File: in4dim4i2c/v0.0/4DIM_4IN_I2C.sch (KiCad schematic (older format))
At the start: 71 parts, among them IC1 ATTINY2313-P, IC2 MOC3020M, IC3 MOC3020M, IC4 MOC3020M, IC5 MOC3020M, P1 CONN_2, P10 CONN_2, P2 CONN_2, P4 CONN_5, P5 CONN_5, P6 CONN_5, P7 CONN_2, P8 CONN_2, P9 CONN_2, U1 TRIAC, U2 TRIAC, U3 TRIAC, U4 TRIAC

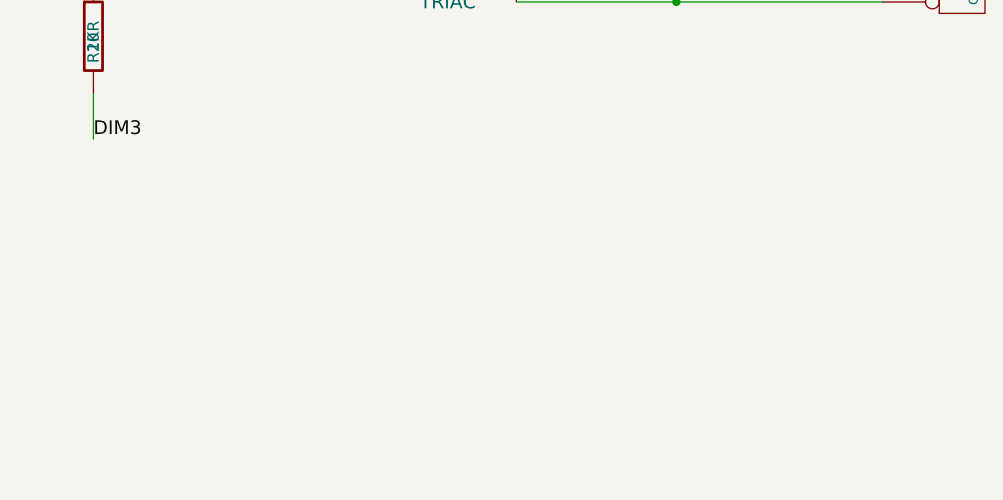
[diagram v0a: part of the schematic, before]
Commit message: Add zero cross detection circuit and P620 footprint
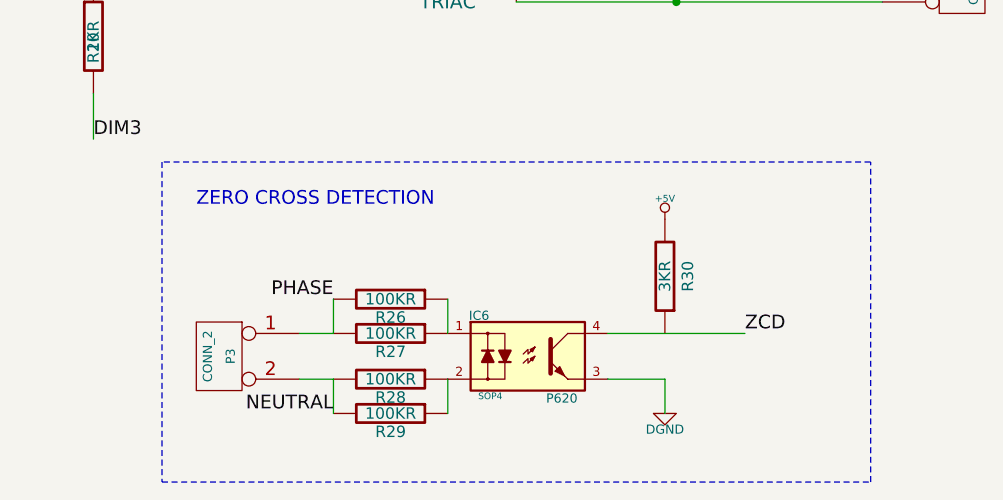
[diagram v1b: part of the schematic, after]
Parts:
- added IC6: P620, SOP4, symbol TLP290
- added P3: CONN_2, symbol CONN_2
- added R26, R27, R28, R29: 100KR, symbol R
- added R30: 3KR, symbol R
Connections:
- net +5V: now also R30.2
- net DGND: now also IC6.3
- net ZCD: now also IC6.4
- new net: IC6.1, R26.1, R27.1
- new net: IC6.2, R28.1, R29.1
- new net NEUTRAL: P3.2 (PM), R28.2, R29.2
- new net PHASE: P3.1 (P1), R26.2, R27.2
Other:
- note added: "ZERO CROSS DETECTION"
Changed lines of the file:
@@
-EESchema Schematic File Version 2  date ven. 17 août 2012 10:03:27 CEST
+EESchema Schematic File Version 2  date sam. 18 août 2012 18:40:52 CEST
 LIBS:power
 LIBS:device
@@
 Sheet 1 1
 Title "16 Digital Inputs Multiplexied Board"
-Date "17 aug 2012"
+Date "18 aug 2012"
 Rev "draft"
 Comp "XPLDUINO project"
@@
 Text Label 13350 2050 0    60   ~ 0
 HT03
+$Comp
+L TLP290 IC6
+U 1 1 502FC400
+P 12500 9600
+F 0 "IC6" H 12287 9778 40  0000 C CNN
+F 1 "P620" H 12649 9416 40  0000 C CNN
+F 2 "SOP4" H 12336 9426 29  0000 C CNN
+	1    12500 9600
+	1    0    0    -1
+$EndComp
+$Comp
+L CONN_2 P3
+U 1 1 502FC40D
+P 11150 9600
+F 0 "P3" V 11100 9600 40  0000 C CNN
+F 1 "CONN_2" V 11200 9600 40  0000 C CNN
+	1    11150 9600
+	-1   0    0    -1
+$EndComp
+$Comp
+L R R27
+U 1 1 502FC413
+P 11900 9500
+F 0 "R27" V 11980 9500 50  0000 C CNN
+F 1 "100KR" V 11900 9500 50  0000 C CNN
+	1    11900 9500
+	0    1    1    0
+$EndComp
+$Comp
+L R R26
+U 1 1 502FC419
+P 11900 9350
+F 0 "R26" V 11980 9350 50  0000 C CNN
+F 1 "100KR" V 11900 9350 50  0000 C CNN
+	1    11900 9350
+	0    1    1    0
+$EndComp
+$Comp
+L R R28
+U 1 1 502FC41F
+P 11900 9700
+F 0 "R28" V 11980 9700 50  0000 C CNN
+F 1 "100KR" V 11900 9700 50  0000 C CNN
+	1    11900 9700
+	0    1    1    0
+$EndComp
+$Comp
+L R R29
+U 1 1 502FC425
+P 11900 9850
+F 0 "R29" V 11980 9850 50  0000 C CNN
+F 1 "100KR" V 11900 9850 50  0000 C CNN
+	1    11900 9850
+	0    1    1    0
+$EndComp
+Wire Wire Line
+	11650 9500 11650 9350
+Wire Wire Line
+	12150 9350 12150 9500
+Wire Wire Line
+	12150 9850 12150 9700
+Wire Wire Line
+	11650 9850 11650 9700
+$Comp
+L R R30
+U 1 1 502FC6AC
+P 13100 9250
+F 0 "R30" V 13000 9250 50  0000 C CNN
+F 1 "3KR" V 13100 9250 50  0000 C CNN
+	1    13100 9250
+	-1   0    0    1
+$EndComp
+Wire Wire Line
+	12850 9500 13450 9500
+Wire Wire Line
+	12850 9700 13100 9700
+Wire Wire Line
+	13100 9700 13100 9850
+$Comp
+L DGND #PWR041
+U 1 1 502FC913
+P 13100 9850
+F 0 "#PWR041" H 13100 9850 40  0001 C CNN
+F 1 "DGND" H 13100 9780 40  0000 C CNN
+	1    13100 9850
+	1    0    0    -1
+$EndComp
+$Comp
+L +5V #PWR042
+U 1 1 502FC919
+P 13100 9000
+F 0 "#PWR042" H 13100 9090 20  0001 C CNN
+F 1 "+5V" H 13100 9090 30  0000 C CNN
+	1    13100 9000
+	1    0    0    -1
+$EndComp
+Text Label 13450 9500 0    60   ~ 0
+ZCD
+Wire Notes Line
+	10900 8750 10900 10150
+Wire Notes Line
+	10900 10150 14000 10150
+Wire Notes Line
+	14000 10150 14000 8750
+Wire Notes Line
+	14000 8750 10900 8750
+Text Notes 11050 8950 0    60   ~ 0
+ZERO CROSS DETECTION
+Wire Wire Line
+	11500 9500 11650 9500
+Wire Wire Line
+	11650 9700 11500 9700
+Text Label 11650 9350 2    60   ~ 0
+PHASE
+Text Label 11650 9850 2    60   ~ 0
+NEUTRAL
 $EndSCHEMATC

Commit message: routage pcb (suite)
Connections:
- net GATE0: now reaches IC2.4, U1.3
- net GATE1: now reaches IC3.4, U2.3
- net GATE2: now reaches IC4.4, U3.3
- net GATE3: now reaches IC5.4, U4.3
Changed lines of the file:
@@
-EESchema Schematic File Version 2  date sam. 18 août 2012 18:40:52 CEST
+EESchema Schematic File Version 2  date mar. 21 août 2012 13:58:49 CEST
 LIBS:power
 LIBS:device
@@
 Sheet 1 1
 Title "16 Digital Inputs Multiplexied Board"
-Date "18 aug 2012"
+Date "21 aug 2012"
 Rev "draft"
 Comp "XPLDUINO project"
@@
 	1    0    0    -1
 $EndComp
-Wire Wire Line
-	11850 1250 12450 1250
 Wire Wire Line
 	12450 1250 12450 1400
@@
 Text Label 11650 9850 2    60   ~ 0
 NEUTRAL
+Wire Wire Line
+	11850 1250 12450 1250
+Text Label 11500 1450 0    60   ~ 0
+GATE0
+Text Label 11550 3400 0    60   ~ 0
+GATE1
+Text Label 11600 5500 0    60   ~ 0
+GATE2
+Text Label 11600 7450 0    60   ~ 0
+GATE3
 $EndSCHEMATC

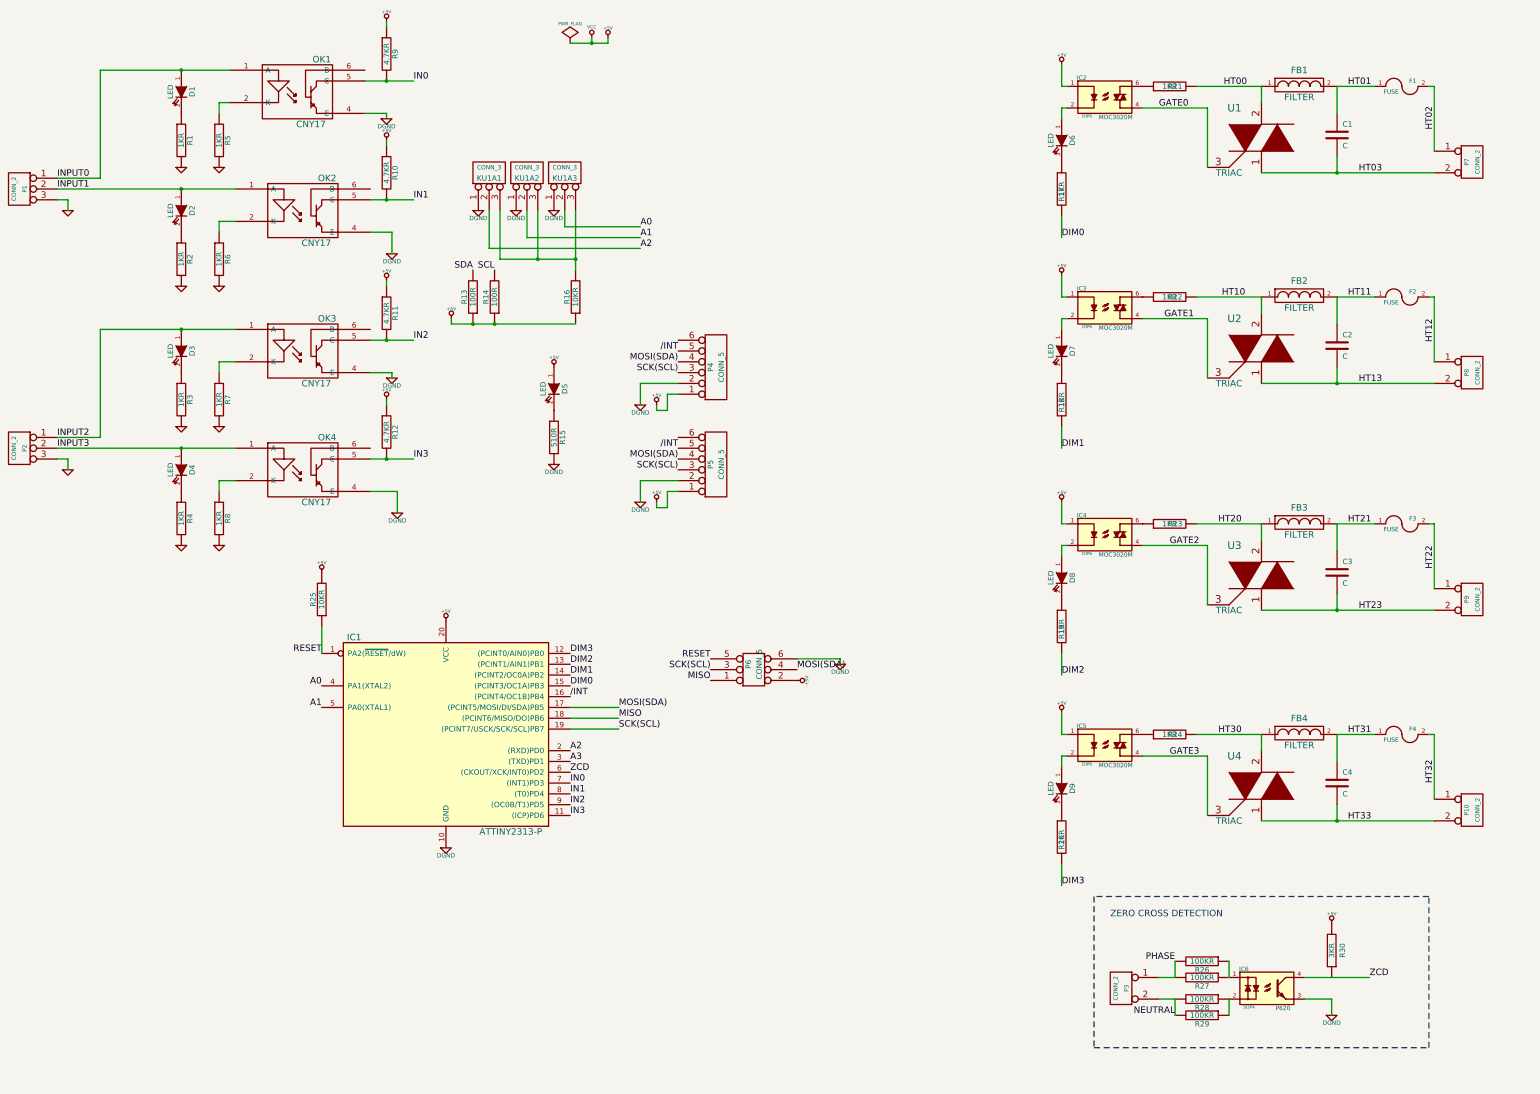
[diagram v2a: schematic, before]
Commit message: Add status led Optimize the routing Ready for review
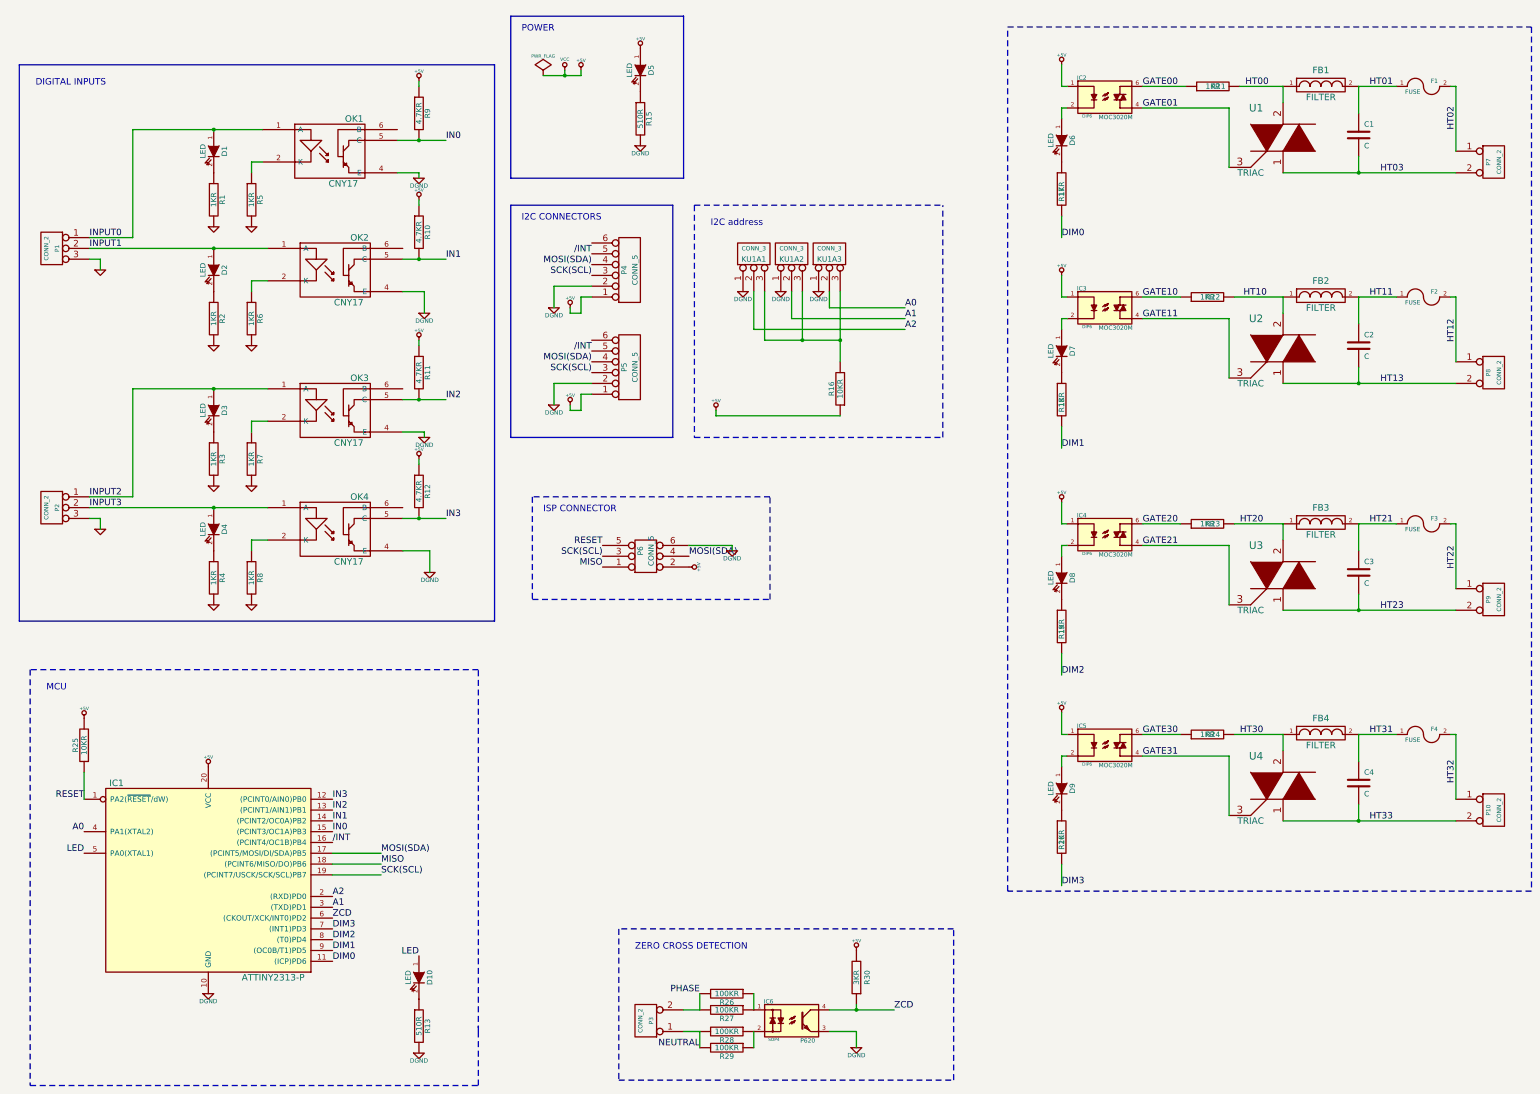
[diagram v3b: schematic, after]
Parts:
- removed R14: 100R, symbol R
- added D10: LED, symbol LED
- R13: value 100R -> 510R
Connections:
- net A3 is gone; now on net A1: IC1.3 ((TXD)PD1)
- net SDA is gone; now on net DGND: R13.2
- net +5V: no longer R13.1
- net A1: no longer IC1.5 (PA0(XTAL1))
- net DIM0: now also IC1.11 ((ICP)PD6); no longer IC1.15 ((PCINT3/OC1A)PB3)
- net DIM1: now also IC1.9 ((OC0B/T1)PD5); no longer IC1.14 ((PCINT2/OC0A)PB2)
- net DIM2: now also IC1.8 ((T0)PD4); no longer IC1.13 ((PCINT1/AIN1)PB1)
- net DIM3: now also IC1.7 ((INT1)PD3); no longer IC1.12 ((PCINT0/AIN0)PB0)
- net IN0: now also IC1.15 ((PCINT3/OC1A)PB3); no longer IC1.7 ((INT1)PD3)
- net IN1: now also IC1.14 ((PCINT2/OC0A)PB2); no longer IC1.8 ((T0)PD4)
- net IN2: now also IC1.13 ((PCINT1/AIN1)PB1); no longer IC1.9 ((OC0B/T1)PD5)
- net IN3: now also IC1.12 ((PCINT0/AIN0)PB0); no longer IC1.11 ((ICP)PD6)
- net NEUTRAL: now also P3.1 (P1); no longer P3.2 (PM)
- net PHASE: now also P3.2 (PM); no longer P3.1 (P1)
- net ZCD: now also R30.1
- net GATE00: now reaches IC2.6, R21.1
- net GATE10: now reaches IC3.6, R22.1
- net GATE20: now reaches IC4.6, R23.1
- net GATE30: now reaches IC5.6, R24.1
- net GATE0 renamed GATE01
- net GATE1 renamed GATE11
- net GATE2 renamed GATE21
- net GATE3 renamed GATE31
- new net: D10.2 (K), R13.1
- new net LED: D10.1 (A), IC1.5 (PA0(XTAL1))
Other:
- note added: "DIGITAL INPUTS"
- note added: "I2C CONNECTORS"
- note added: "I2C address"
- note added: "ISP CONNECTOR"
- note added: "MCU"
- note added: "POWER"
- moved on the sheet: C1, C2, C3, C4, D1, D2, D3, D4, D5, F1, F2, F3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

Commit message: Add selector for the autonomious mode configuration
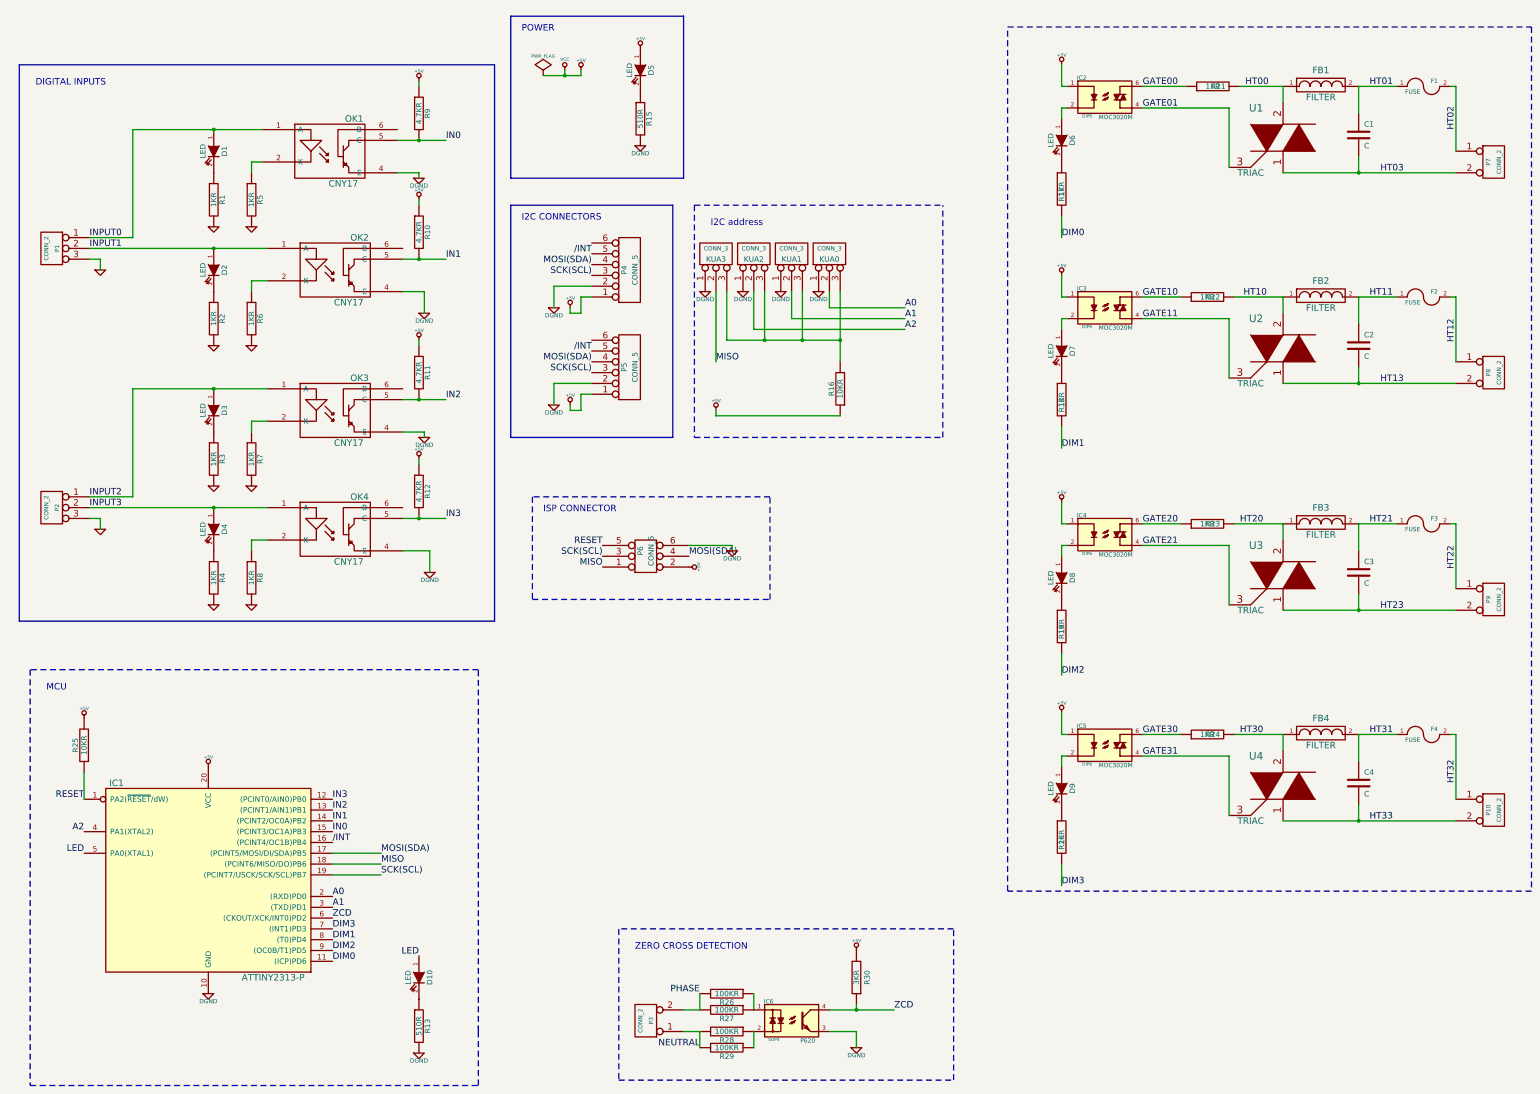
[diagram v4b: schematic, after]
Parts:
- added KUA3: CONN_3, symbol CONN_3
- renumbered KU1A3 to KUA0, KU1A2 to KUA1, KU1A1 to KUA2
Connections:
- net A0: now also IC1.2 ((RXD)PD0); no longer IC1.4 (PA1(XTAL2))
- net A2: now also IC1.4 (PA1(XTAL2)); no longer IC1.2 ((RXD)PD0)
- net DGND: now also KUA3.1 (P1)
- net DIM1: now also IC1.8 ((T0)PD4); no longer IC1.9 ((OC0B/T1)PD5)
- net DIM2: now also IC1.9 ((OC0B/T1)PD5); no longer IC1.8 ((T0)PD4)
- net MISO: now also KUA3.2 (PM)
- net at KUA0.3 (P3), KUA1.3 (P3), KUA2.3 (P3)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: now also KUA3.3 (P3)
